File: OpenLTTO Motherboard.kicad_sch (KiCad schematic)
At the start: 17 parts, among them J1 MBUS, Q1 IRLML6244

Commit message: Updated schematic metadata, and added PCB renders, and schematic PDF
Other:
- company: (none) -> Paul Mumby
- title: (none) -> OpenLTTO Motherboard
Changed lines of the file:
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@@
 (kicad_sch (version 20230121) (generator eeschema)
   (paper "A4")
+  (title_block
+    (title "OpenLTTO Motherboard")
+    (rev "1.0")
+    (company "Paul Mumby")
+  )
   (junction (at 140.97 121.92) (diameter 0) (color 0 0 0 0)
   )

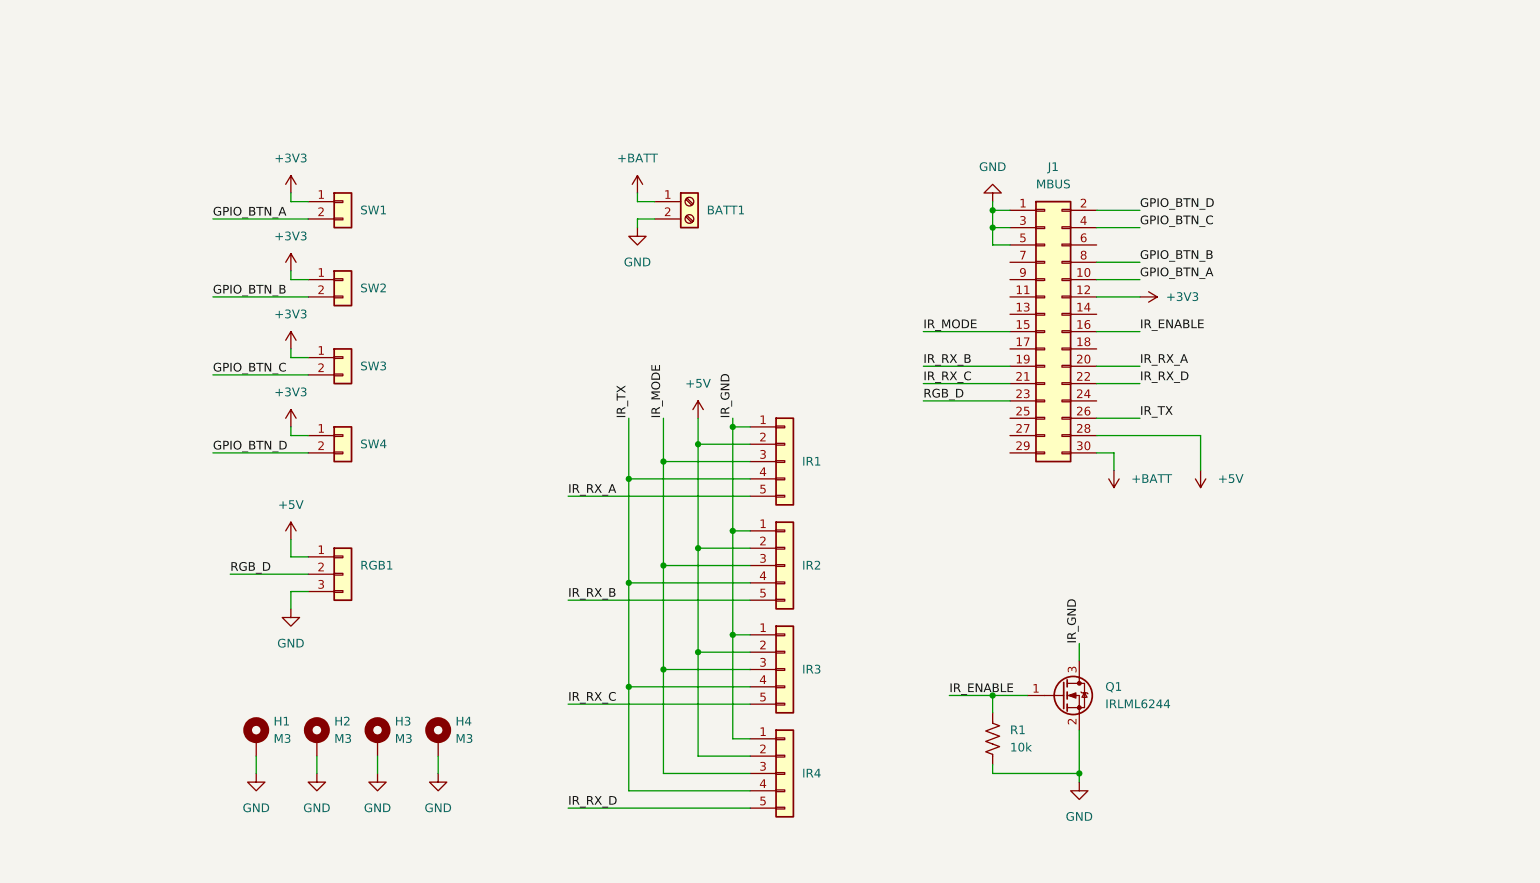
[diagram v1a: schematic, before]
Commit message: Updated Schematic to v1.1, added GPIO breakout and changed IR ports to all be independent. Also added I2C port, and added license, and updated readme
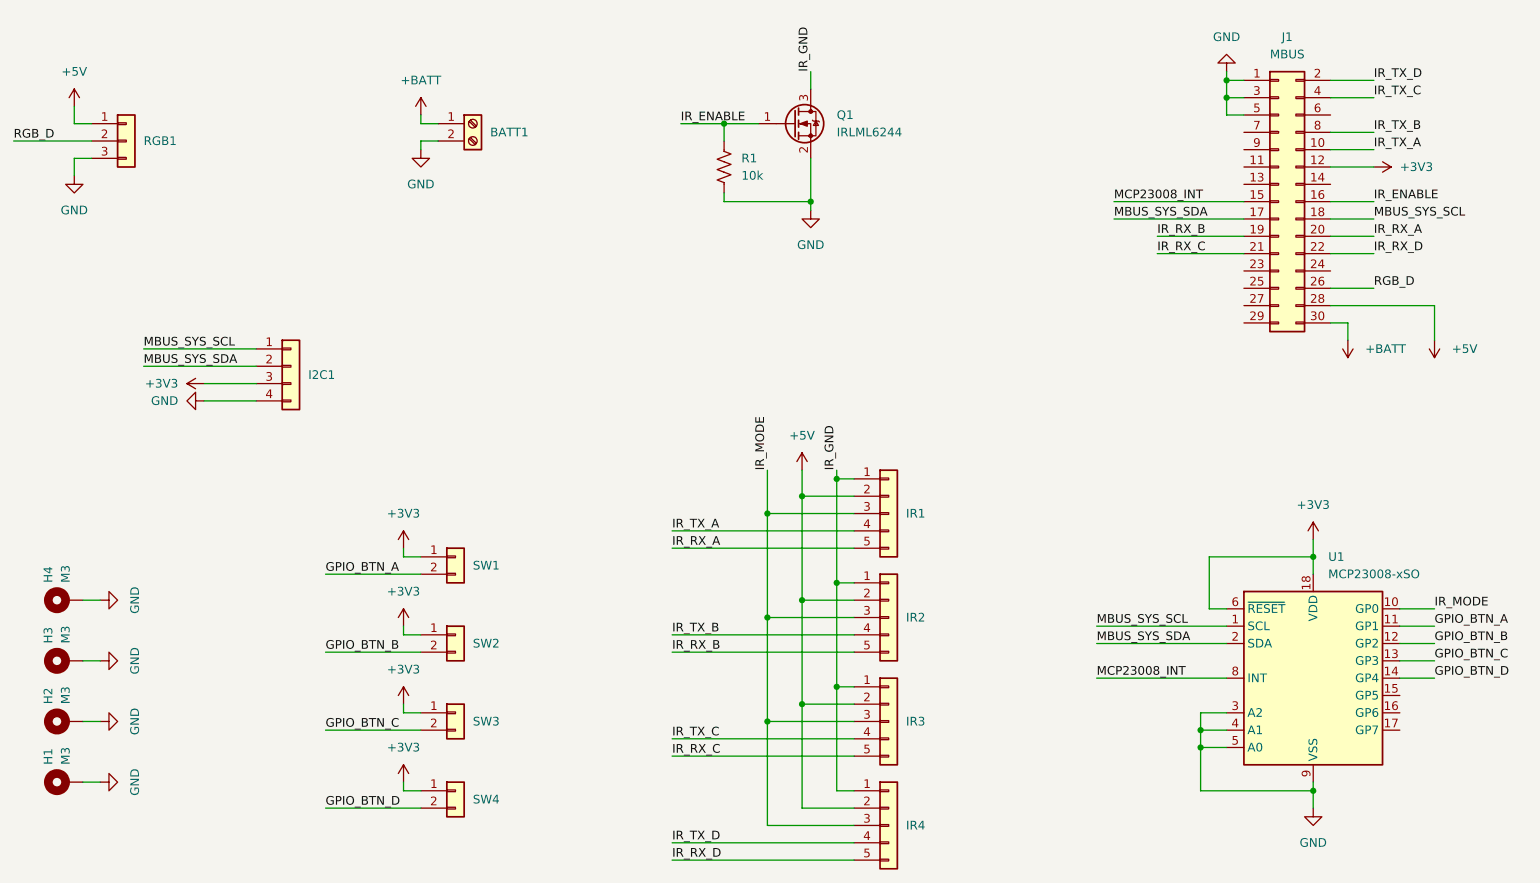
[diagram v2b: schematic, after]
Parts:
- added I2C1: ~, Connector_JST:JST_PH_B4B-PH-K_1x04_P2.00mm_Vertical, symbol Connector_Generic:Conn_01x04
- added U1: MCP23008-xSO, Package_SO:SOIC-18W_7.5x11.6mm_P1.27mm, symbol Interface_Expansion:MCP23008-xSO
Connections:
- net +3V3: now also I2C1.3 (Pin_3), U1.18 (VDD), U1.6 (~{RESET})
- net GND: now also I2C1.4 (Pin_4), U1.3 (A2), U1.4 (A1), U1.5 (A0), U1.9 (VSS)
- net GPIO_BTN_A: now also U1.11 (GP1); no longer J1.10 (Pin_10)
- net GPIO_BTN_B: now also U1.12 (GP2); no longer J1.8 (Pin_8)
- net GPIO_BTN_C: now also U1.13 (GP3); no longer J1.4 (Pin_4)
- net GPIO_BTN_D: now also U1.14 (GP4); no longer J1.2 (Pin_2)
- net IR_MODE: now also U1.10 (GP0); no longer J1.15 (Pin_15)
- net RGB_D: now also J1.26 (Pin_26); no longer J1.23 (Pin_23)
- net MBUS_SYS_SDA: now reaches J1.17 (Pin_17)
- net MBUS_SYS_SDA: now also I2C1.2 (Pin_2), U1.2 (SDA)
- net MBUS_SYS_SCL: now reaches J1.18 (Pin_18)
- net MBUS_SYS_SCL: now also I2C1.1 (Pin_1), U1.1 (SCL)
- removed net IR_TX: IR1.4 (Pin_4), IR2.4 (Pin_4), IR3.4 (Pin_4), IR4.4 (Pin_4), J1.26 (Pin_26)
- new net IR_TX_A: IR1.4 (Pin_4), J1.10 (Pin_10)
- new net IR_TX_B: IR2.4 (Pin_4), J1.8 (Pin_8)
- new net IR_TX_C: IR3.4 (Pin_4), J1.4 (Pin_4)
- new net IR_TX_D: IR4.4 (Pin_4), J1.2 (Pin_2)
- new net MCP23008_INT: J1.15 (Pin_15), U1.8 (INT)
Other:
- moved on the sheet: BATT1, H1, H2, H3, H4, IR1, IR2, IR3, IR4, J1, Q1, R1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
